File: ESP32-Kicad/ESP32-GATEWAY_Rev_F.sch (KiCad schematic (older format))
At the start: 59 parts, among them J1 Conn_01x07_Male, T1 DTC114YKA, U2 TLV62569DBVT(SOT23-5), U3 ESP32-WROOM-32D-4MB, U4 LAN8710A-EZC(QFN32)

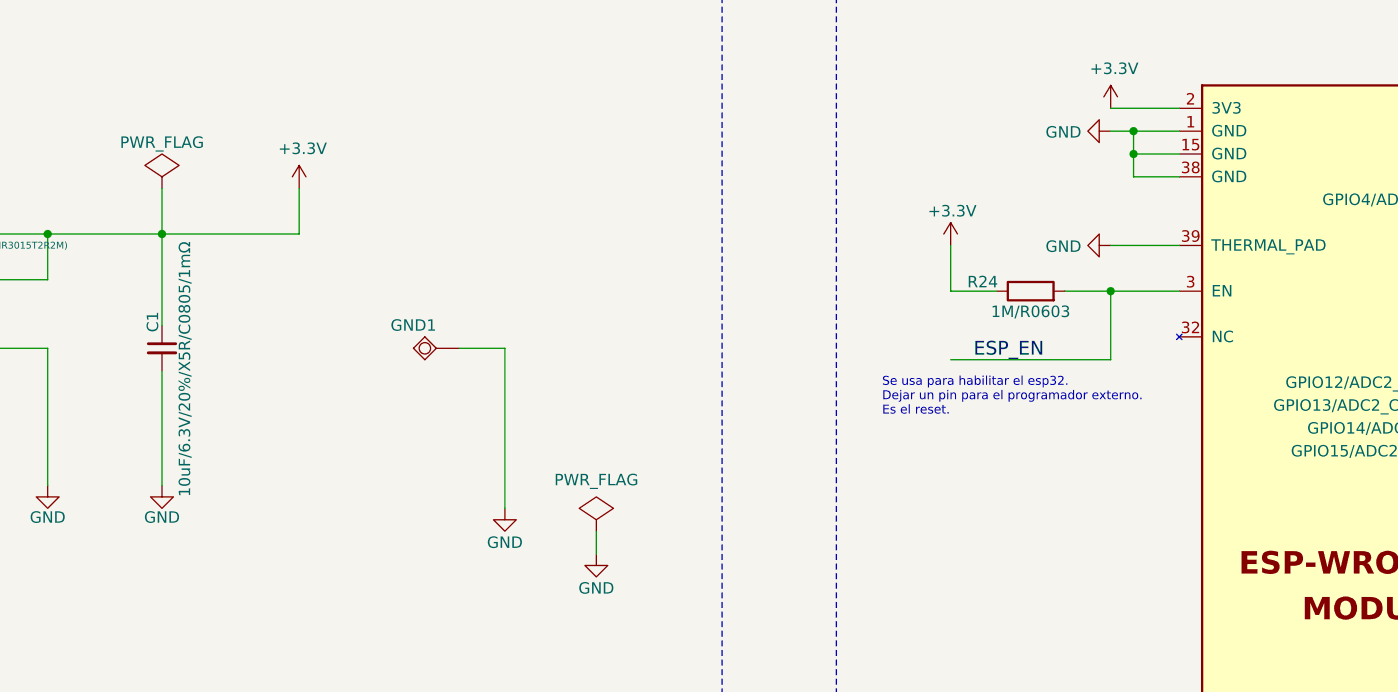
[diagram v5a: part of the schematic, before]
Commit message: Proyecto en kicad actualizado
Push button agregado, se acomodaron los sensores y se agregó un capacitor a la salida de la fuente
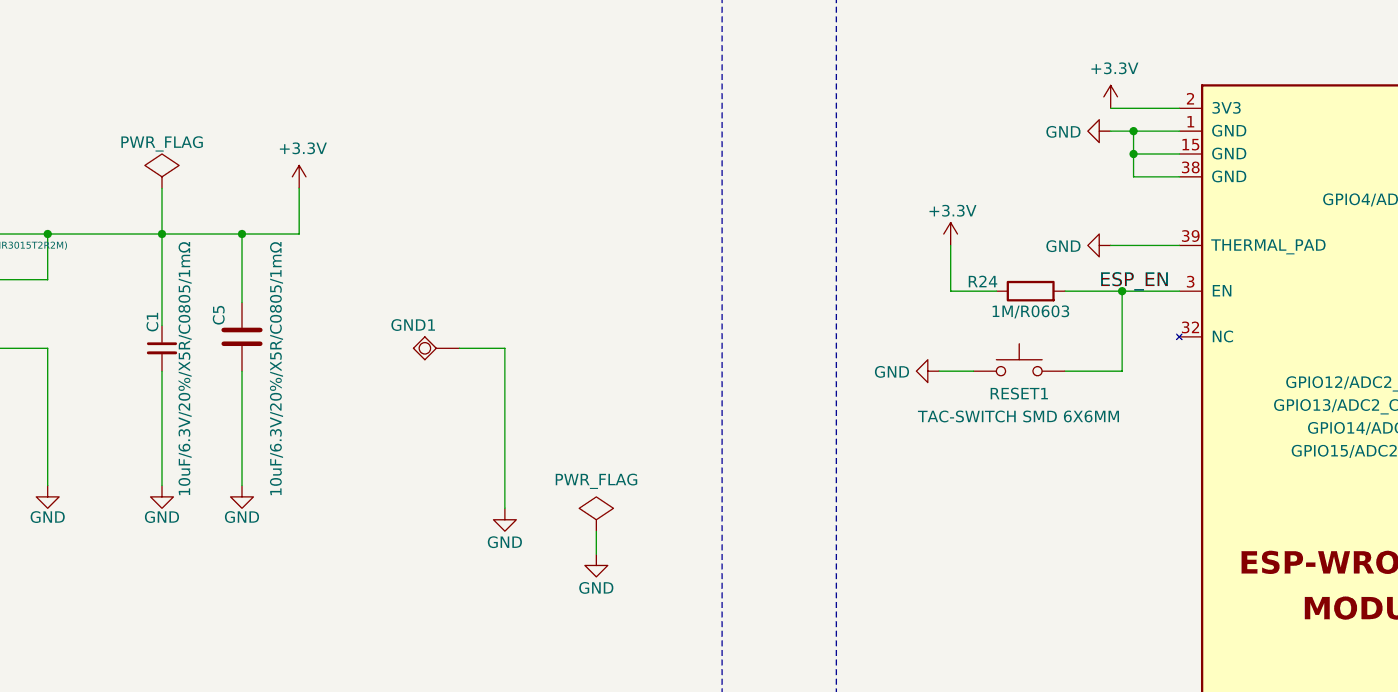
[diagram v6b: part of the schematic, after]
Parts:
- added C5: 10uF/6.3V/20%/X5R/C0805/1mΩ, Capacitor_SMD:C_0805_2012Metric_Pad1.18x1.45mm_HandSolder, symbol Device:C
- added RESET1: TAC-SWITCH SMD 6X6MM, Button_Switch_SMD:SW_SPST_PTS645, symbol Switch:SW_Push
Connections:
- wire segments 287 -> 291
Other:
- note removed: "Se usa para habilitar el esp32.\nDejar un pin para el programador externo.\nEs el reset."
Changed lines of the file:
@@
 	1    0    0    -1
 $EndComp
-Text Label 10600 3000 0    60   ~ 0
+Text Label 11150 2700 0    60   ~ 0
 ESP_EN
 Text Label 15600 4700 0    50   ~ 0
@@
 	10000 700  10000 5500
 Wire Wire Line
-	11200 3000 10500 3000
-Wire Wire Line
 	6700 9200 6700 9100
 Connection ~ 6700 8400
@@
 Wire Wire Line
 	6500 5900 8500 5900
-Wire Wire Line
-	11000 2700 11200 2700
-Wire Wire Line
-	11200 2700 11200 3000
-Connection ~ 11200 2700
 Wire Wire Line
 	8000 10500 8500 10500
@@
 	7050 2450 7050 2850
 Wire Wire Line
-	7050 2450 7650 2450
+	7050 2450 7400 2450
 Wire Wire Line
 	6550 2450 7050 2450
@@
 Wire Wire Line
 	6700 10000 6700 10600
-Wire Wire Line
-	11200 2700 11500 2700
 Wire Wire Line
 	1800 8800 1900 8800
@@
 Connection ~ 3500 6800
 Connection ~ 3500 6500
-Text Notes 10200 3250 0    39   ~ 0
-Se usa para habilitar el esp32.\nDejar un pin para el programador externo.\nEs el reset.
 Text Notes 16750 3400 0    39   ~ 0
 (logs)\n
@@
 Wire Wire Line
 	20550 2900 21900 2900
+$Comp
+L ESP32-GATEWAY_Rev_F:GND #PWR0108
+U 1 1 612BD481
+P 10450 3050
+F 0 "#PWR0108" H 10450 2800 50  0001 C CNN
+F 1 "GND" V 10455 2922 50  0000 R CNN
+F 2 "" H 10450 3050 60  0000 C CNN
+F 3 "" H 10450 3050 60  0000 C CNN
+	1    10450 3050
+	0    1    1    0
+$EndComp
+Wire Wire Line
+	11000 3050 11250 3050
+Wire Wire Line
+	10600 3050 10450 3050
+Wire Wire Line
+	11000 2700 11250 2700
+Wire Wire Line
+	11250 3050 11250 2700
+Connection ~ 11250 2700
+Wire Wire Line
+	11250 2700 11500 2700
+$Comp
+L Device:C C5
+U 1 1 6126FE78
+P 7400 2900
+F 0 "C5" V 7300 2950 50  0000 L CNN
+F 1 "10uF/6.3V/20%/X5R/C0805/1mΩ" V 7550 2200 50  0000 L CNN
+F 2 "Capacitor_SMD:C_0805_2012Metric_Pad1.18x1.45mm_HandSolder" H 7438 2750 50  0001 C CNN
+F 3 "~" H 7400 2900 50  0001 C CNN
+	1    7400 2900
+	1    0    0    -1
+$EndComp
+Wire Wire Line
+	7400 2750 7400 2450
+Connection ~ 7400 2450
+Wire Wire Line
+	7400 2450 7650 2450
+$Comp
+L ESP32-GATEWAY_Rev_F:GND #PWR0109
+U 1 1 612A65DA
+P 7400 3550
+F 0 "#PWR0109" H 7400 3300 50  0001 C CNN
+F 1 "GND" H 7400 3410 50  0000 C CNN
+F 2 "" H 7400 3550 60  0000 C CNN
+F 3 "" H 7400 3550 60  0000 C CNN
+	1    7400 3550
+	1    0    0    -1
+$EndComp
+Wire Wire Line
+	7400 3050 7400 3550
+$Comp
+L Switch:SW_Push RESET1
+U 1 1 613A766A
+P 10800 3050
+F 0 "RESET1" H 10800 2950 50  0000 C CNN
+F 1 "TAC-SWITCH SMD 6X6MM" H 10800 2850 50  0000 C CNN
+F 2 "Button_Switch_SMD:SW_SPST_PTS645" H 10800 3250 50  0001 C CNN
+F 3 "~" H 10800 3250 50  0001 C CNN
+	1    10800 3050
+	1    0    0    -1
+$EndComp
 $EndSCHEMATC

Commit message: Placa kicad actualizada
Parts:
- added R40, R41: 440/R0603, Resistor_SMD:R_0603_1608Metric_Pad0.98x0.95mm_HandSolder, symbol Device:R
- added U1, U5: ACPL-217-56AE, Package_SO:SO-4_4.4x2.3mm_P1.27mm, symbol Isolator:SFH617A-1
- DOOR1, DOOR2: value Conn_01x02_Female -> Conn_01x02
- TEMP1, TEMP2: value Conn_01x03_Female -> Conn_01x03
- USB-UART2: symbol Connector:USB_B_Micro -> ESP32-GATEWAY_Rev_F-rescue:USB_B_Micro-Connector
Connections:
- wire segments 291 -> 301
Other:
- moved on the sheet: C1, C11, C12, C13, C14, C15, C16, C17, C18, C19, C2, C20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

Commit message: Proyecto en kicad actualizado
Esquemático actualizado
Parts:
- L2: value 2.2uH/1.5A/DCR=35mR/20%/3.00x3.00x1.50mm/CD32(NR3015T2R2M) -> 2.2uH/9A/DCR=35mR/20%/3.00x3.00x1.50mm/CD32(NR3015T2R2M); footprint OLIMEX_RLC-FP:CD32 -> footprints_personales:SMD_0530
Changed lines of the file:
@@
 P 8150 4400
 F 0 "L2" H 8150 4500 50  0000 C CNN
-F 1 "2.2uH/1.5A/DCR=35mR/20%/3.00x3.00x1.50mm/CD32(NR3015T2R2M)" H 8300 4350 30  0000 C CNN
-F 2 "OLIMEX_RLC-FP:CD32" H 8100 4400 60  0001 C CNN
+F 1 "2.2uH/9A/DCR=35mR/20%/3.00x3.00x1.50mm/CD32(NR3015T2R2M)" H 8300 4350 30  0000 C CNN
+F 2 "footprints_personales:SMD_0530" H 8100 4400 60  0001 C CNN
 F 3 "" H 8100 4400 60  0000 C CNN
 	1    8150 4400
